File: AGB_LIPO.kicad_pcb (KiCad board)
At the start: 2 copper layers, 52 x 23 mm, 5 parts, among them J1 Conn_01x02_Male, U1 tp4056_board-tp4056

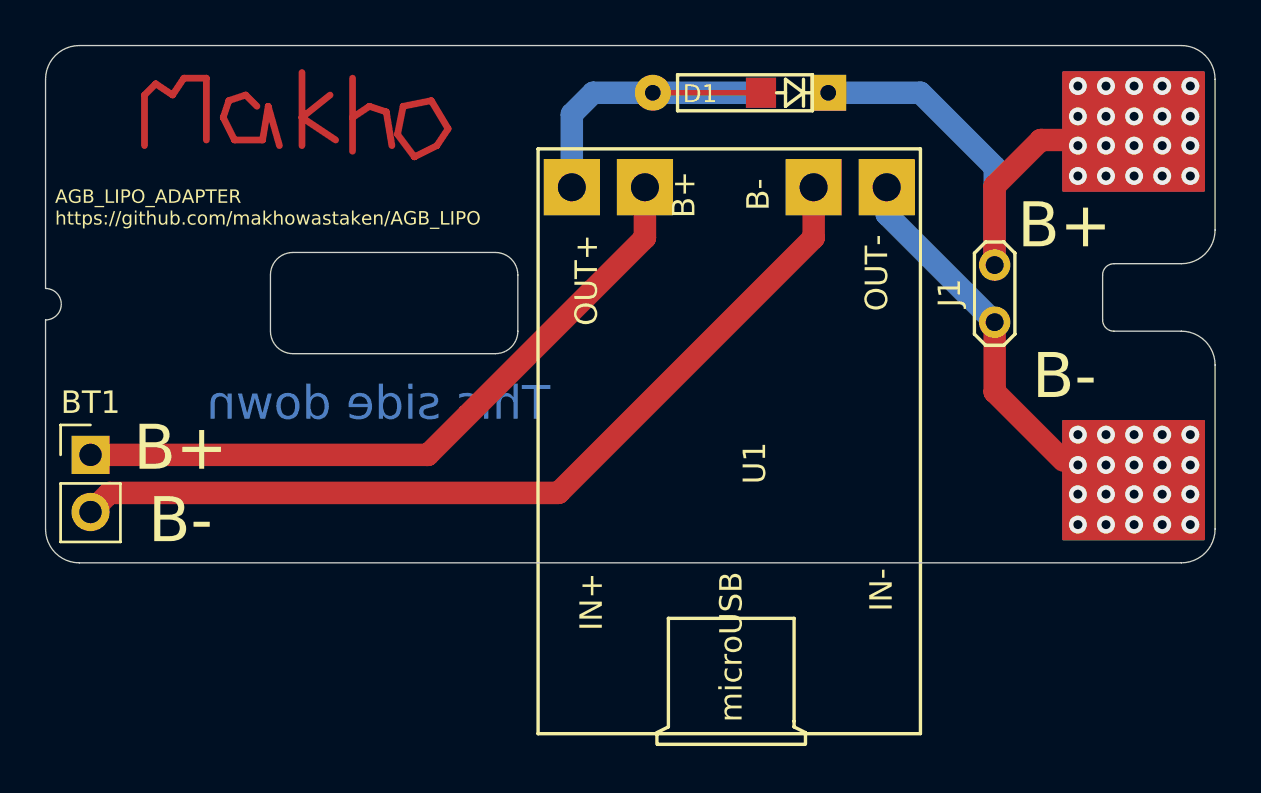
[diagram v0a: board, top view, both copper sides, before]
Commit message: Add files via upload
tweaked the dimensions to fit better
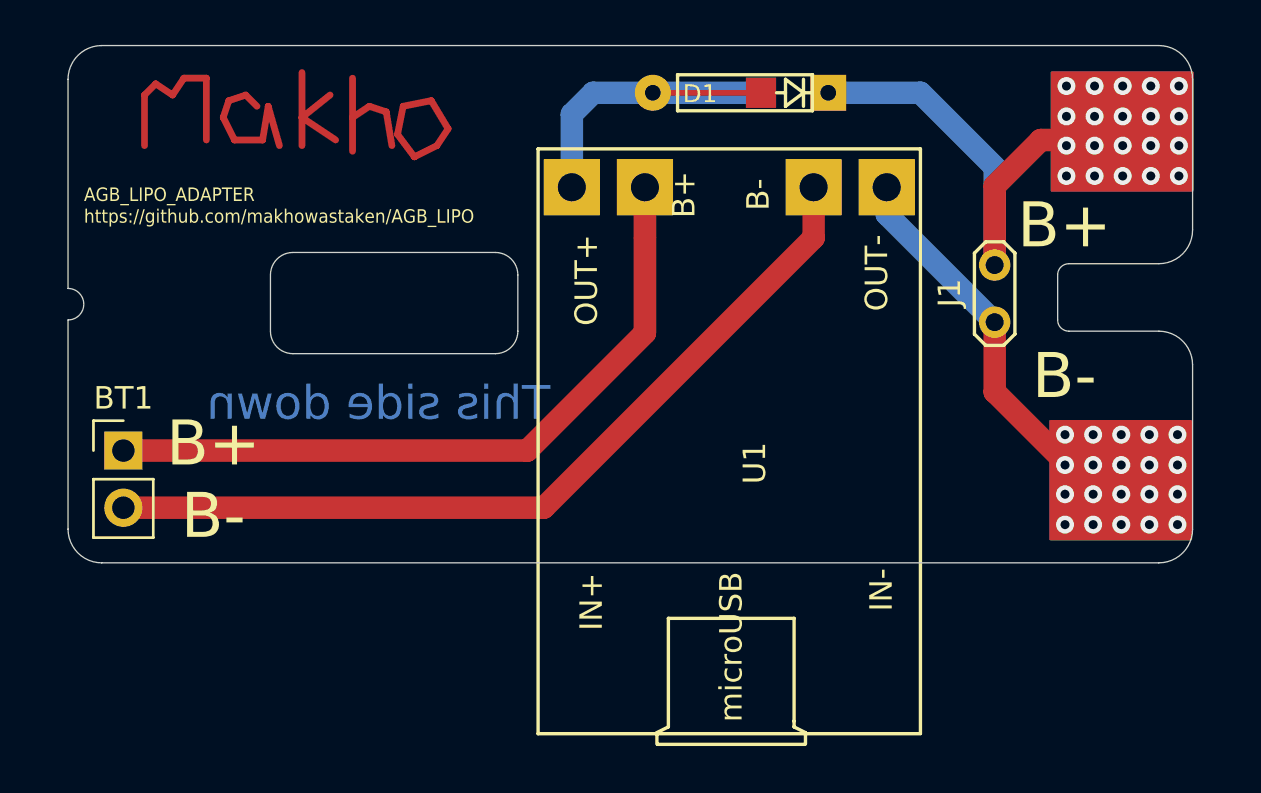
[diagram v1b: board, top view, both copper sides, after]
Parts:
- moved BT1 1.47 mm to (78.5, 37.3)
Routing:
- net Net-(BT1-Pad2): track 39.4 -> 37.9 mm
- net Net-(BT1-Pad1): track 30.9 -> 31.8 mm
- net Net-(J1-Pad1): vias 0 -> 1
- net Net-(D1-Pad1): vias 2 -> 3
- net (no net): vias 38 -> 36
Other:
- board size 52 x 23 mm -> 50 x 23 mm

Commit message: Add files via upload
modified placement of components on board, updated silkscreen and soldermask to represent updated files
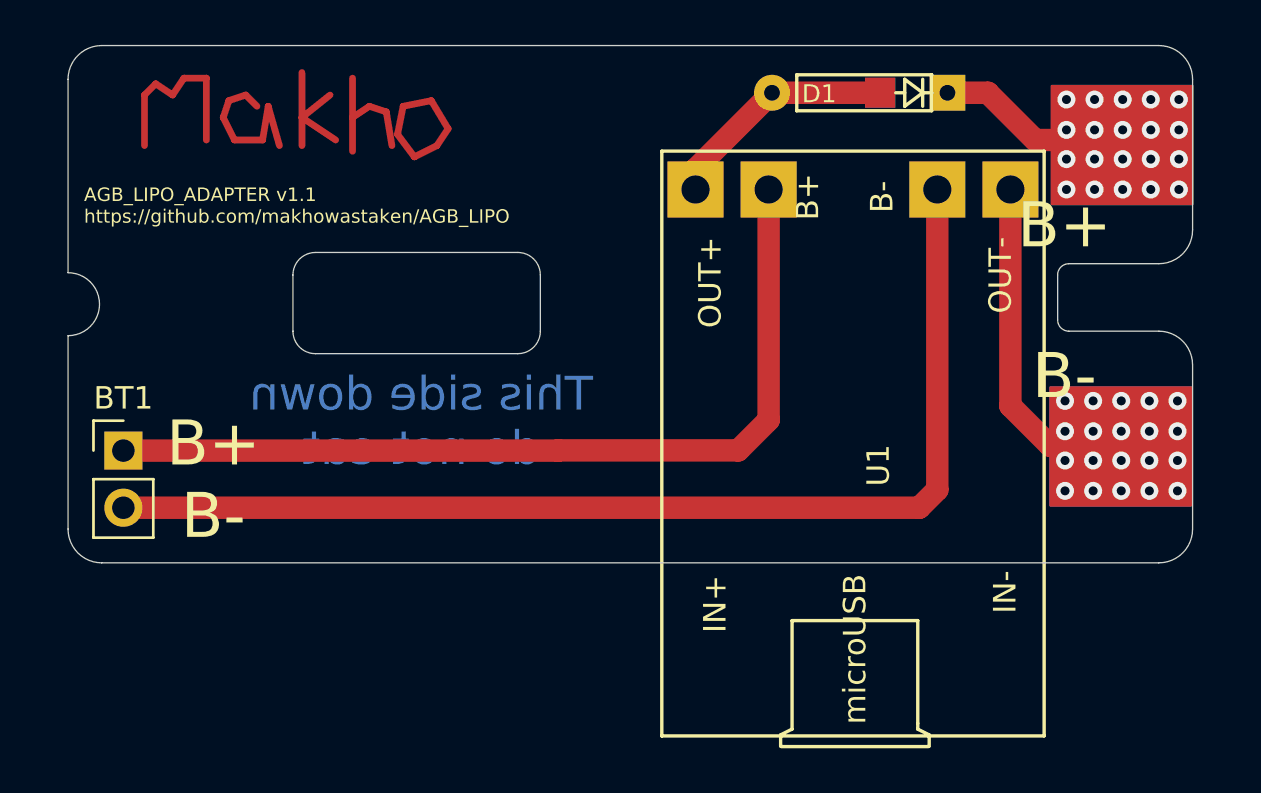
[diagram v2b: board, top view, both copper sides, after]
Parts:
- removed J1: Conn_01x02_Male, TestPoint:TestPoint_2Pads_Pitch2.54mm_Drill0.8mm
- moved U1 5.50 mm to (110.9, 36.7)
- moved D1 5.30 mm to (111.2, 21.4)
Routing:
- net Net-(D1-Pad1): track 22.8 -> 8.57 mm, vias 3 -> 6
- net Net-(BT1-Pad2): track 37.9 -> 49.9 mm
- net Net-(BT1-Pad1): track 31.8 -> 39.5 mm
- net Net-(D1-Pad2): track 12.1 -> 10.5 mm
- net Net-(J1-Pad1): vias 1 -> 6
- net (no net): vias 36 -> 28
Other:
- outline, holes or cut-outs redrawn
- board text added: "AGB_LIPO_ADAPTER v1.1 https://github.com/makhowastaken/AGB_LIPO"
- board text added: "This side down do not eat"
- board text removed: "AGB_LIPO_ADAPTER https://github.com/makhowastaken/AGB_LIPO"
- board text removed: "This side down"
